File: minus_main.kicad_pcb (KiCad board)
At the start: 2 copper layers, 177.8 x 86.4 mm, 7 parts, among them P1 CONN_01X05, P2 CONN_02X04, P3 CONN_01X02, U1 socket_leon_x3_dil64, U2 socket_pololu_24v12, U3 socket_pololu_24v12, U4 socket_lm2596_mod

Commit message: minus: h-bridge: switch to DFRobot L298P shield
previously, pololu were on schematic.

Signed-off-by: Yannick Gicquel <ygicquel@gmail.com>
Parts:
- removed U2, U3: socket_pololu_24v12, bot_parts:pololu_24v12_dip
- added SHIELD1: arduino_shield, arduino_shields:arduino_shield, F.Cu at (124.5, 146.0)

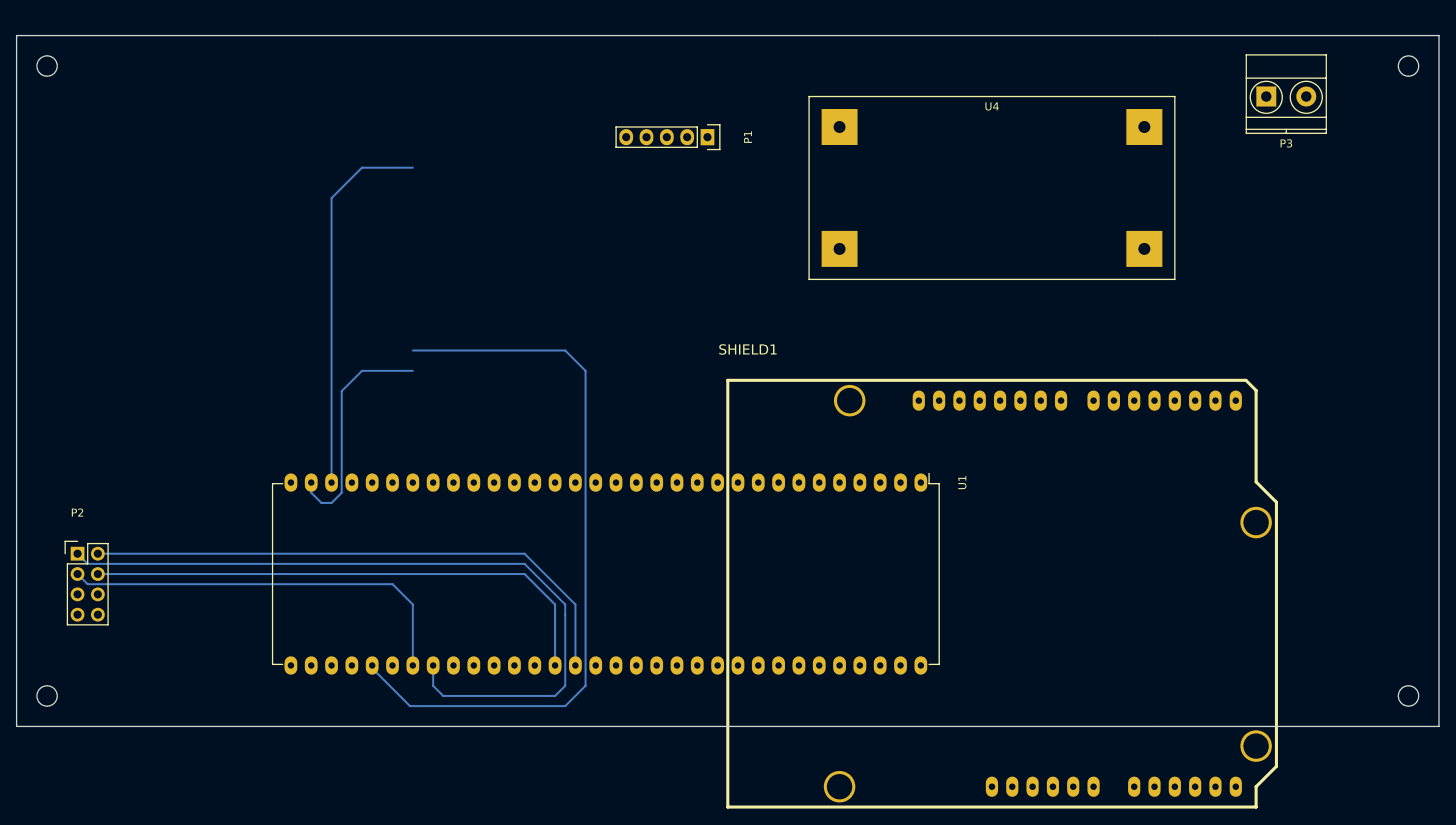
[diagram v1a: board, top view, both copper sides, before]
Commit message: minus: add encoder connectors
pcb update

Signed-off-by: Yannick Gicquel <ygicquel@gmail.com>
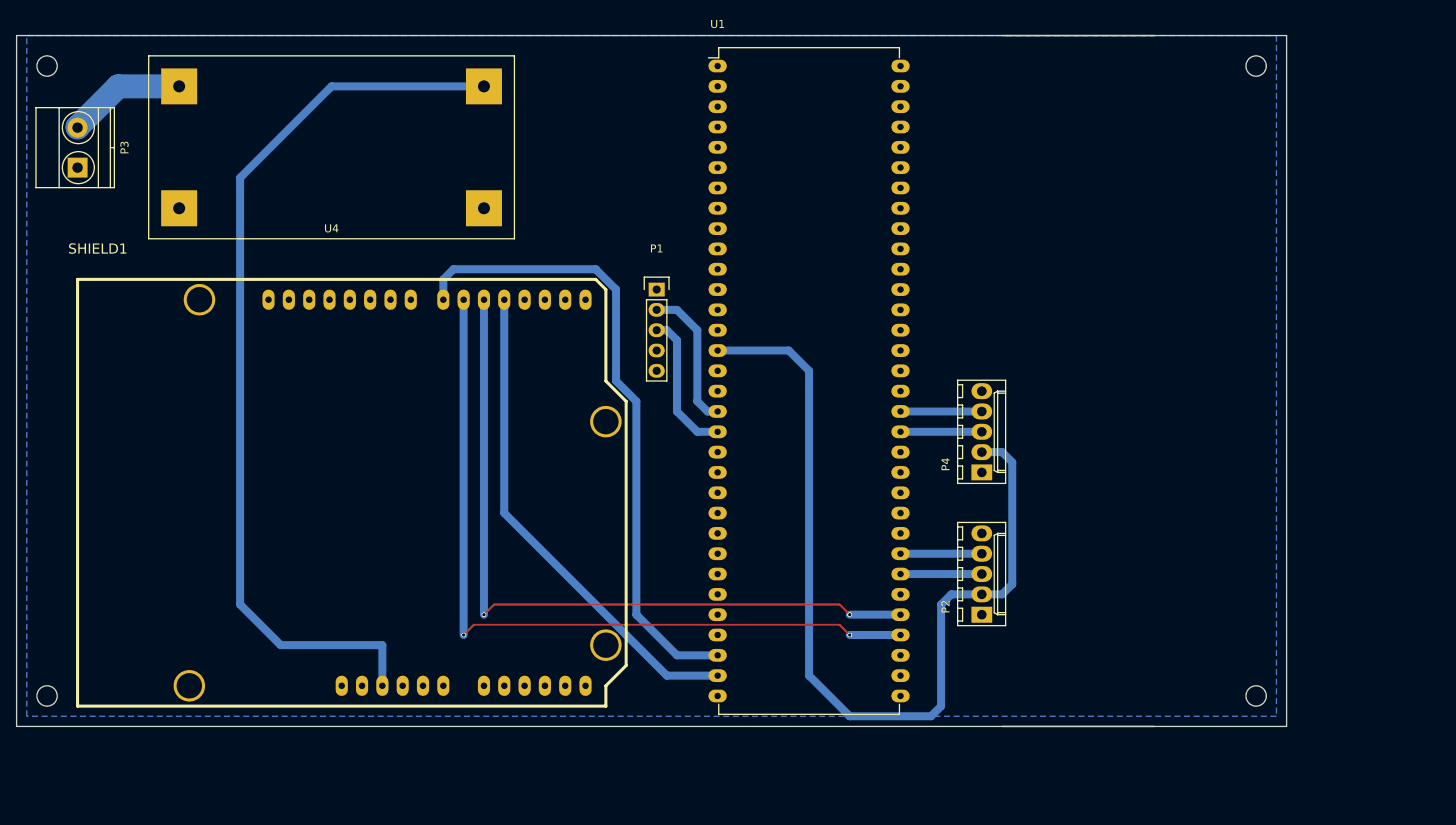
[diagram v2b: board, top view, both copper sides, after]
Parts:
- added P4: CONN_01X05, Connectors_Molex:Molex_KK-6410-05_05x2.54mm_Straight, F.Cu at (156.2, 104.1)
- P2: value CONN_02X04 -> CONN_01X05; footprint Pin_Headers:Pin_Header_Straight_2x04 -> Connectors_Molex:Molex_KK-6410-05_05x2.54mm_Straight
- moved P3 148.9 mm to (43.2, 66.0), turned to 90 degrees
- moved P2 113.3 mm to (156.2, 121.9), turned to 90 degrees
- moved U4 82.7 mm to (74.9, 63.5), turned to 0 degrees
- moved SHIELD1 82.3 mm to (43.2, 133.3)
- moved U1 57.9 mm to (123.2, 53.3), turned to 0 degrees
- moved P1 20.1 mm to (115.6, 81.3), turned to 0 degrees
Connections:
- P2 pad 1: ENCB_L -> GND
- P2 pad 2: ENCB_R -> +3V3
- P2 pad 4: ENCA_R -> ENCB_L
- P2 pad 5: +3V3 -> Net-(P2-Pad5)
- U1 pad 14: Net-(U1-Pad14) -> GND
- U1 pad 15: Net-(U1-Pad15) -> +3V3
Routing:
- net +5V: track 0.00 -> 113.5 mm
- net +3V3: track 0.00 -> 111.9 mm
- net /Sheet_MCU/PWM_L: track 0.35 -> 97.6 mm, vias 0 -> 2
- net ENCB_L: track 93.9 -> 10.2 mm
- net ENCB_R: track 69.9 -> 10.2 mm
- net ENCA_R: track 66.3 -> 10.2 mm
- net ENCA_L: track 51.1 -> 10.2 mm
- net /Sheet_MCU/DIR_R: track 28.8 -> 61.8 mm
- net /Sheet_MCU/DIR_L: track 47.3 -> 79.7 mm
- net /Sheet_Connectors/UART_DBG_RXD: track 0.00 -> 18.1 mm
- net /Sheet_Connectors/UART_DBG_TXD: track 0.00 -> 18.1 mm
- net +24V: track 0.00 -> 14.9 mm
- net /Sheet_MCU/PWM_R: track 92.0 -> 92.5 mm, vias 0 -> 2
- added copper zone on B.Cu, net GND
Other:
- board size 177.8 x 86.4 mm -> 158.8 x 86.4 mm

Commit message: minus: add 3V3 module on schematic & pcb
Signed-off-by: Yannick Gicquel <ygicquel@gmail.com>
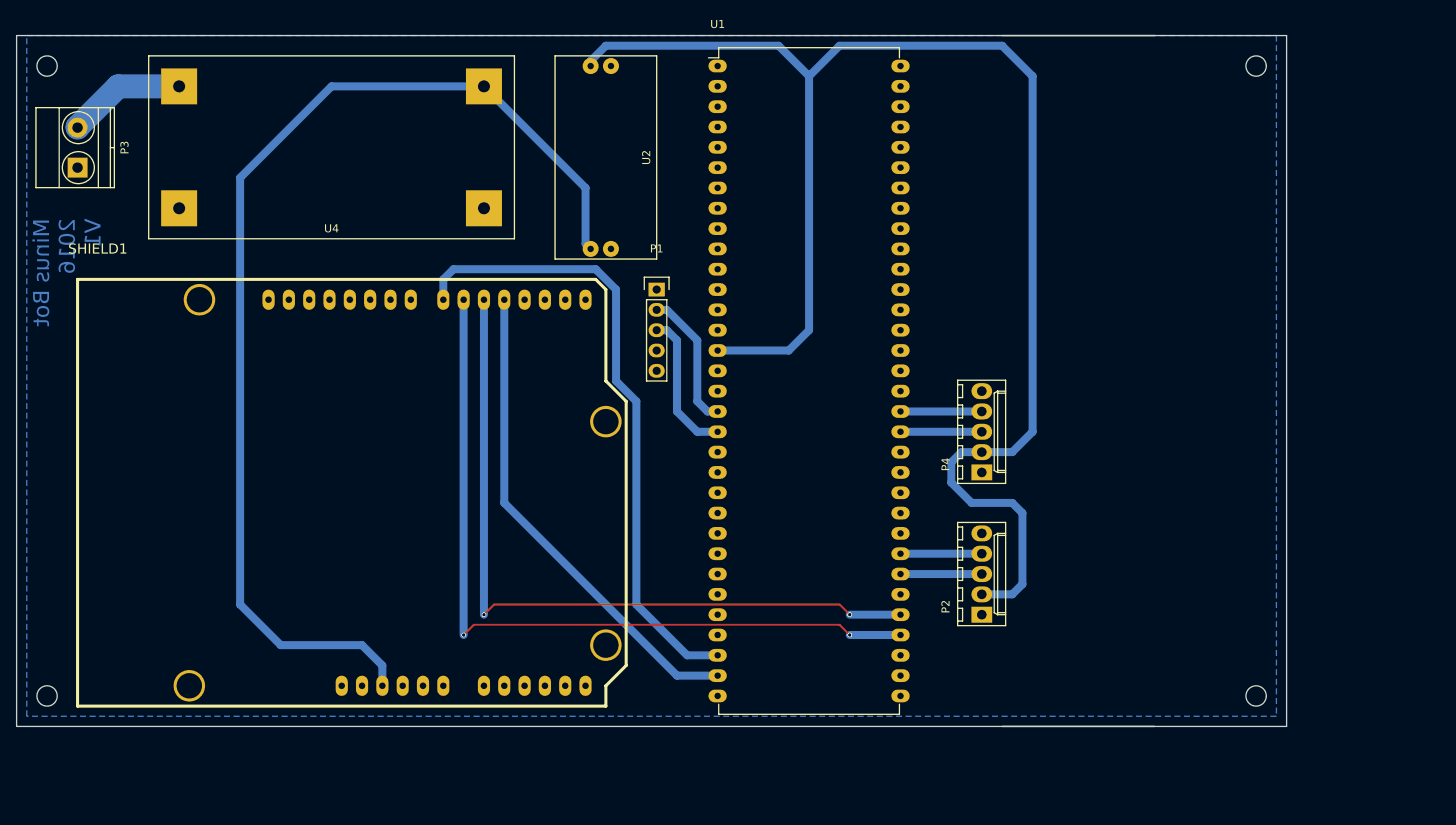
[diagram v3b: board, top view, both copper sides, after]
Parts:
- added U2: socket_ams1117-3V3_mod, bot_parts:ams1117-3V3_mod, F.Cu at (109.2, 64.8)
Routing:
- net +3V3: track 111.9 -> 189.3 mm
- net +5V: track 113.5 -> 137.9 mm
- net /Sheet_MCU/DIR_L: track 79.7 -> 78.9 mm
- net /Sheet_MCU/DIR_R: track 61.8 -> 61.0 mm
- net /Sheet_Connectors/UART_DBG_TXD: track 18.1 -> 17.3 mm
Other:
- board text added: "Minus Bot 2016 V1"
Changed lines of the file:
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@@
 (kicad_pcb (version 4) (host pcbnew 4.0.4+e1-6308~48~ubuntu16.04.1-stable)
   (general
-    (links 22)
-    (no_connects 2)
+    (links 26)
+    (no_connects 0)
     (area 35.484999 49.454999 194.385001 135.965001)
     (thickness 1.6)
-    (drawings 10)
-    (tracks 62)
+    (drawings 11)
+    (tracks 75)
     (zones 0)
-    (modules 7)
+    (modules 8)
     (nets 92)
   )
@@
       (net 90 "Net-(P2-Pad5)"))
   )
+  (module bot_parts:ams1117-3V3_mod (layer F.Cu)
+    (at 109.22 64.77 90)
+    (fp_text reference U2 (at 0 5.08 90) (layer F.SilkS)
+      (effects (font (size 1 1) (thickness 0.15)))
+    )
+    (fp_text value socket_ams1117-3V3_mod (at 0 -5.08 90) (layer F.Fab)
+      (effects (font (size 1 1) (thickness 0.15)))
+    )
+    (fp_line (start -12.7 -6.35) (end 12.7 -6.35) (layer F.SilkS) (width 0.15))
+    (fp_line (start 12.7 -6.35) (end 12.7 6.35) (layer F.SilkS) (width 0.15))
+    (fp_line (start 12.7 6.35) (end -12.7 6.35) (layer F.SilkS) (width 0.15))
+    (fp_line (start -12.7 6.35) (end -12.7 -6.35) (layer F.SilkS) (width 0.15))
+    (pad 1 thru_hole circle (at -11.43 -1.905 90) (size 2 2) (drill 0.8) (layers *.Cu *.Mask)
+      (net 68 +5V))
+    (pad 2 thru_hole circle (at -11.43 0.635 90) (size 2 2) (drill 0.8) (layers *.Cu *.Mask)
+      (net 54 GND))
+    (pad 3 thru_hole circle (at 11.43 -1.905 90) (size 2 2) (drill 0.8) (layers *.Cu *.Mask)
+      (net 55 +3V3))
+    (pad 4 thru_hole circle (at 11.43 0.635 90) (size 2 2) (drill 0.8) (layers *.Cu *.Mask)
+      (net 54 GND))
+  )
+  (gr_text "Minus Bot\n2016\nV1" (at 41.91 72.39 90) (layer B.Cu)
+    (effects (font (size 2 2) (thickness 0.375)) (justify left mirror))
+  )
   (gr_circle (center 39.37 53.34) (end 40.64 53.34) (layer Edge.Cuts) (width 0.15))
   (gr_circle (center 190.5 53.34) (end 190.5 52.07) (layer Edge.Cuts) (width 0.15))
@@
   (segment (start 43.18 60.96) (end 48.26 55.88) (width 3) (layer B.Cu) (net 53))
   (segment (start 48.26 55.88) (end 55.88 55.88) (width 3) (layer B.Cu) (net 53))
-  (segment (start 156.21 101.6) (end 158.75 101.6) (width 1) (layer B.Cu) (net 55))
+  (segment (start 156.21 101.6) (end 153.67 101.6) (width 1) (layer B.Cu) (net 55) (status 400000))
+  (segment (start 160.02 119.38) (end 156.21 119.38) (width 1) (layer B.Cu) (net 55) (status 800000))
+  (segment (start 161.29 118.11) (end 160.02 119.38) (width 1) (layer B.Cu) (net 55))
+  (segment (start 161.29 109.22) (end 161.29 118.11) (width 1) (layer B.Cu) (net 55))
+  (segment (start 160.02 107.95) (end 161.29 109.22) (width 1) (layer B.Cu) (net 55))
+  (segment (start 154.94 107.95) (end 160.02 107.95) (width 1) (layer B.Cu) (net 55))
+  (segment (start 152.4 105.41) (end 154.94 107.95) (width 1) (layer B.Cu) (net 55))
+  (segment (start 152.4 102.87) (end 152.4 105.41) (width 1) (layer B.Cu) (net 55))
+  (segment (start 153.67 101.6) (end 152.4 102.87) (width 1) (layer B.Cu) (net 55))
+  (segment (start 134.62 54.61) (end 138.43 50.8) (width 1) (layer B.Cu) (net 55))
+  (segment (start 160.02 101.6) (end 156.21 101.6) (width 1) (layer B.Cu) (net 55) (status 800000))
+  (segment (start 162.56 99.06) (end 160.02 101.6) (width 1) (layer B.Cu) (net 55))
+  (segment (start 162.56 54.61) (end 162.56 99.06) (width 1) (layer B.Cu) (net 55))
+  (segment (start 158.75 50.8) (end 162.56 54.61) (width 1) (layer B.Cu) (net 55))
+  (segment (start 138.43 50.8) (end 158.75 50.8) (width 1) (layer B.Cu) (net 55))
+  (segment (start 132.08 88.9) (end 134.62 86.36) (width 1) (layer B.Cu) (net 55))
+  (segment (start 109.22 50.8) (end 107.315 52.705) (width 1) (layer B.Cu) (net 55) (status 800000))
+  (segment (start 130.81 50.8) (end 109.22 50.8) (width 1) (layer B.Cu) (net 55))
+  (segment (start 134.62 54.61) (end 130.81 50.8) (width 1) (layer B.Cu) (net 55))
+  (segment (start 134.62 86.36) (end 134.62 54.61) (width 1) (layer B.Cu) (net 55))
+  (segment (start 107.315 52.705) (end 107.315 53.34) (width 1) (layer B.Cu) (net 55) (status C00000))
   (segment (start 132.08 88.9) (end 123.19 88.9) (width 1) (layer B.Cu) (net 55))
-  (segment (start 134.62 91.44) (end 132.08 88.9) (width 1) (layer B.Cu) (net 55))
-  (segment (start 134.62 129.54) (end 134.62 91.44) (width 1) (layer B.Cu) (net 55))
-  (segment (start 139.7 134.62) (end 134.62 129.54) (width 1) (layer B.Cu) (net 55))
-  (segment (start 149.86 134.62) (end 139.7 134.62) (width 1) (layer B.Cu) (net 55))
-  (segment (start 151.13 133.35) (end 149.86 134.62) (width 1) (layer B.Cu) (net 55))
-  (segment (start 151.13 120.65) (end 151.13 133.35) (width 1) (layer B.Cu) (net 55))
-  (segment (start 152.4 119.38) (end 151.13 120.65) (width 1) (layer B.Cu) (net 55))
-  (segment (start 158.75 119.38) (end 152.4 119.38) (width 1) (layer B.Cu) (net 55))
-  (segment (start 160.02 118.11) (end 158.75 119.38) (width 1) (layer B.Cu) (net 55))
-  (segment (start 160.02 102.87) (end 160.02 118.11) (width 1) (layer B.Cu) (net 55))
-  (segment (start 158.75 101.6) (end 160.02 102.87) (width 1) (layer B.Cu) (net 55))
-  (segment (start 115.57 83.82) (end 118.11 83.82) (width 1) (layer B.Cu) (net 57))
+  (segment (start 115.57 83.82) (end 116.84 83.82) (width 1) (layer B.Cu) (net 57) (status 400000))
   (segment (start 121.92 96.52) (end 123.19 96.52) (width 1) (layer B.Cu) (net 57))
   (segment (start 120.65 95.25) (end 121.92 96.52) (width 1) (layer B.Cu) (net 57))
-  (segment (start 120.65 86.36) (end 120.65 95.25) (width 1) (layer B.Cu) (net 57))
-  (segment (start 118.11 83.82) (end 120.65 86.36) (width 1) (layer B.Cu) (net 57))
+  (segment (start 120.65 87.63) (end 120.65 95.25) (width 1) (layer B.Cu) (net 57))
+  (segment (start 116.84 83.82) (end 120.65 87.63) (width 1) (layer B.Cu) (net 57))
   (segment (start 115.57 86.36) (end 116.84 86.36) (width 1) (layer B.Cu) (net 58))
   (segment (start 120.65 99.06) (end 123.19 99.06) (width 1) (layer B.Cu) (net 58))
@@
   (segment (start 156.21 99.06) (end 146.05 99.06) (width 1) (layer B.Cu) (net 63))
   (segment (start 88.9 82.55) (end 88.9 80.01) (width 1) (layer B.Cu) (net 64))
-  (segment (start 118.11 127) (end 123.19 127) (width 1) (layer B.Cu) (net 64))
-  (segment (start 113.03 121.92) (end 118.11 127) (width 1) (layer B.Cu) (net 64))
-  (segment (start 113.03 95.25) (end 113.03 121.92) (width 1) (layer B.Cu) (net 64))
+  (segment (start 119.38 127) (end 123.19 127) (width 1) (layer B.Cu) (net 64) (status 800000))
+  (segment (start 113.03 120.65) (end 119.38 127) (width 1) (layer B.Cu) (net 64))
+  (segment (start 113.03 95.25) (end 113.03 120.65) (width 1) (layer B.Cu) (net 64))
   (segment (start 110.49 92.71) (end 113.03 95.25) (width 1) (layer B.Cu) (net 64))
   (segment (start 110.49 81.28) (end 110.49 92.71) (width 1) (layer B.Cu) (net 64))
@@
   (segment (start 90.17 78.74) (end 107.95 78.74) (width 1) (layer B.Cu) (net 64))
   (segment (start 88.9 80.01) (end 90.17 78.74) (width 1) (layer B.Cu) (net 64))
-  (segment (start 123.19 129.54) (end 116.84 129.54) (width 1) (layer B.Cu) (net 65))
-  (segment (start 96.52 109.22) (end 96.52 82.55) (width 1) (layer B.Cu) (net 65))
-  (segment (start 116.84 129.54) (end 96.52 109.22) (width 1) (layer B.Cu) (net 65))
+  (segment (start 123.19 129.54) (end 118.11 129.54) (width 1) (layer B.Cu) (net 65) (status 400000))
+  (segment (start 96.52 107.95) (end 96.52 82.55) (width 1) (layer B.Cu) (net 65) (status 800000))
+  (segment (start 118.11 129.54) (end 96.52 107.95) (width 1) (layer B.Cu) (net 65))
   (via (at 139.7 124.46) (size 0.6) (drill 0.4) (layers F.Cu B.Cu) (net 66))
   (segment (start 91.44 82.55) (end 91.44 124.46) (width 1) (layer B.Cu) (net 66))
@@
   (segment (start 139.7 121.92) (end 146.05 121.92) (width 1) (layer B.Cu) (net 67))
   (segment (start 93.98 82.55) (end 93.98 121.92) (width 1) (layer B.Cu) (net 67))
-  (segment (start 93.98 55.88) (end 74.93 55.88) (width 1) (layer B.Cu) (net 68))
-  (segment (start 81.28 125.73) (end 81.28 130.81) (width 1) (layer B.Cu) (net 68))
-  (segment (start 68.58 125.73) (end 81.28 125.73) (width 1) (layer B.Cu) (net 68))
+  (segment (start 81.28 130.81) (end 81.28 128.27) (width 1) (layer B.Cu) (net 68) (status 400000))
+  (segment (start 74.93 55.88) (end 63.5 67.31) (width 1) (layer B.Cu) (net 68))
+  (segment (start 63.5 67.31) (end 63.5 120.65) (width 1) (layer B.Cu) (net 68))
   (segment (start 63.5 120.65) (end 68.58 125.73) (width 1) (layer B.Cu) (net 68))
-  (segment (start 63.5 67.31) (end 63.5 120.65) (width 1) (layer B.Cu) (net 68))
-  (segment (start 74.93 55.88) (end 63.5 67.31) (width 1) (layer B.Cu) (net 68))
+  (segment (start 68.58 125.73) (end 78.74 125.73) (width 1) (layer B.Cu) (net 68))
+  (segment (start 78.74 125.73) (end 81.28 128.27) (width 1) (layer B.Cu) (net 68))
+  (segment (start 74.93 55.88) (end 93.98 55.88) (width 1) (layer B.Cu) (net 68))
+  (segment (start 93.98 55.88) (end 106.68 68.58) (width 1) (layer B.Cu) (net 68) (status 400000))
+  (segment (start 106.68 68.58) (end 106.68 75.565) (width 1) (layer B.Cu) (net 68) (status 800000))
+  (segment (start 106.68 75.565) (end 107.315 76.2) (width 1) (layer B.Cu) (net 68) (status C00000))
   (zone (net 54) (net_name GND) (layer B.Cu) (hatch edge 0.508)
     (connect_pads yes (clearance 1.016))
